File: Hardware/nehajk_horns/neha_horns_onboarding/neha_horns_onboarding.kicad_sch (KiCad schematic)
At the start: 17 parts, among them J1 Conn_01x02_Pin, J2 Conn_01x02_Pin, J3 Conn_01x02_Pin, J4 Conn_01x02_Pin, Q1 IRLZ44N

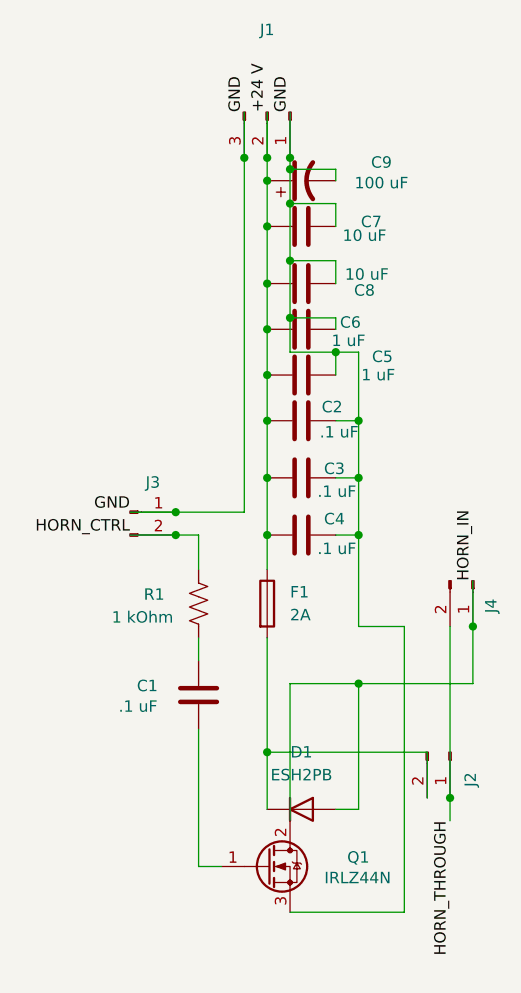
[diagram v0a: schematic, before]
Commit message: Horns PCB with correct connector
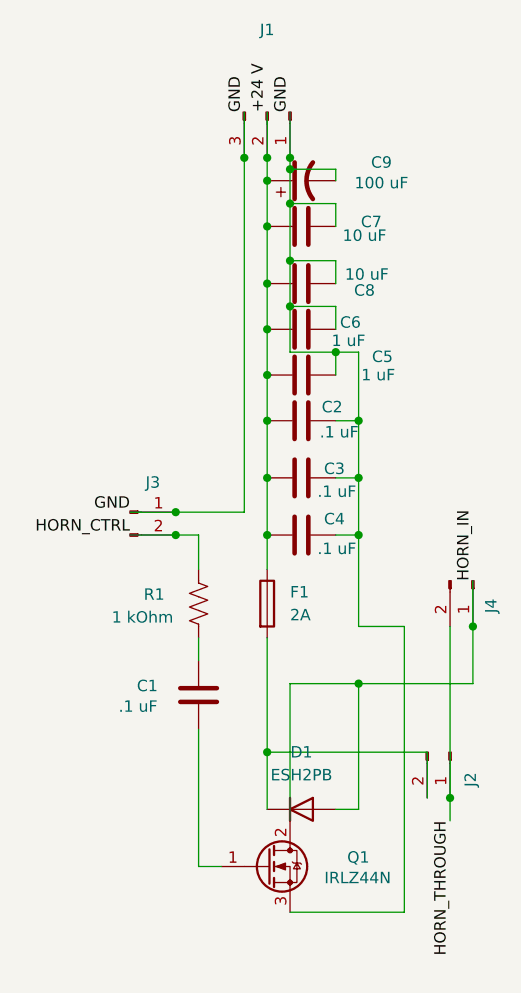
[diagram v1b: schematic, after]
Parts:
- J1: footprint Connector_Molex:Molex_KK-254_AE-6410-03A_1x03_P2.54mm_Vertical -> Connector_Molex:Molex_Micro-Fit_3.0_43650-0300_1x03_P3.00mm_Horizontal
- J2, J3, J4: footprint Connector_Molex:Molex_KK-254_AE-6410-02A_1x02_P2.54mm_Vertical -> Connector_Molex:Molex_Micro-Fit_3.0_43650-0200_1x02_P3.00mm_Horizontal
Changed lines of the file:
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@@
 	)
 	(junction
-		(at 143.51 81.28)
+		(at 143.51 80.01)
 		(diameter 0)
 		(color 0 0 0 0)
@@
 	(wire
 		(pts
-			(xy 143.51 81.28) (xy 143.51 85.09)
+			(xy 143.51 80.01) (xy 143.51 85.09)
 		)
 		(stroke
@@
 	(wire
 		(pts
-			(xy 148.59 81.28) (xy 143.51 81.28)
-		)
-		(stroke
-			(width 0)
-			(type default)
-		)
-	)
-	(wire
-		(pts
-			(xy 143.51 74.93) (xy 143.51 81.28)
+			(xy 148.59 80.01) (xy 143.51 80.01)
+		)
+		(stroke
+			(width 0)
+			(type default)
+		)
+	)
+	(wire
+		(pts
+			(xy 143.51 74.93) (xy 143.51 80.01)
 		)
 		(stroke
@@
 	(wire
 		(pts
-			(xy 148.59 81.28) (xy 148.59 82.55)
+			(xy 148.59 80.01) (xy 148.59 82.55)
 		)
 		(stroke
@@
 			)
 		)
-		(property "Footprint" "Connector_Molex:Molex_KK-254_AE-6410-02A_1x02_P2.54mm_Vertical"
+		(property "Footprint" "Connector_Molex:Molex_Micro-Fit_3.0_43650-0200_1x02_P3.00mm_Horizontal"
 			(at 125.73 102.87 0)
 			(effects
@@
 			)
 		)
-		(property "Footprint" "Connector_Molex:Molex_KK-254_AE-6410-02A_1x02_P2.54mm_Vertical"
+		(property "Footprint" "Connector_Molex:Molex_Micro-Fit_3.0_43650-0200_1x02_P3.00mm_Horizontal"
 			(at 161.29 129.54 0)
 			(effects
@@
 			)
 		)
-		(property "Footprint" "Connector_Molex:Molex_KK-254_AE-6410-02A_1x02_P2.54mm_Vertical"
+		(property "Footprint" "Connector_Molex:Molex_Micro-Fit_3.0_43650-0200_1x02_P3.00mm_Horizontal"
 			(at 163.83 110.49 0)
 			(effects
@@
 			)
 		)
-		(property "Footprint" "Connector_Molex:Molex_KK-254_AE-6410-03A_1x03_P2.54mm_Vertical"
+		(property "Footprint" "Connector_Molex:Molex_Micro-Fit_3.0_43650-0300_1x03_P3.00mm_Horizontal"
 			(at 140.97 58.42 0)
 			(effects

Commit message: corrections made to Horns/LED
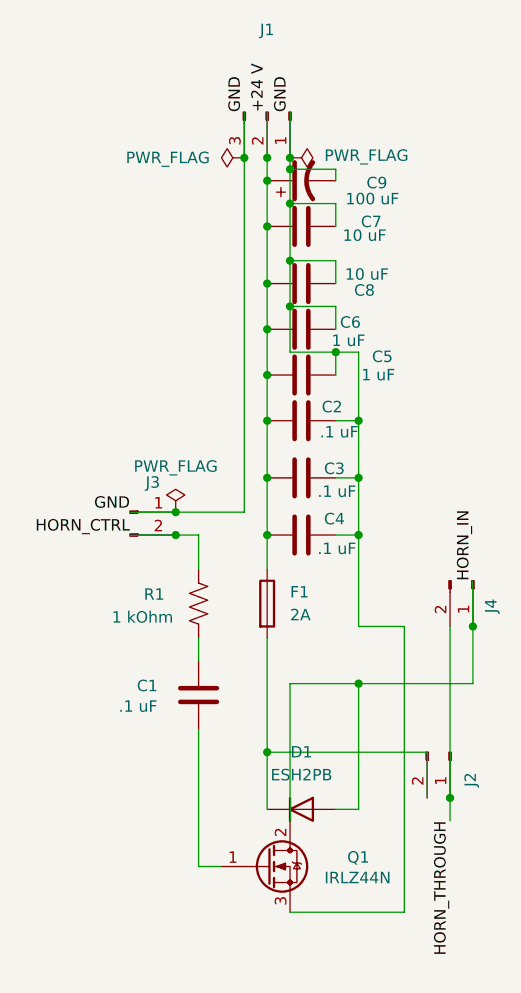
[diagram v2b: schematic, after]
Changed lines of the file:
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@@
+	)
+	(symbol
+		(lib_id "power:PWR_FLAG")
+		(at 138.43 63.5 90)
+		(unit 1)
+		(exclude_from_sim no)
+		(in_bom yes)
+		(on_board yes)
+		(dnp no)
+		(fields_autoplaced yes)
+		(property "Reference" "#FLG2"
+			(at 136.525 63.5 0)
+			(effects
+				(font
+					(size 1.27 1.27)
+				)
+				(hide yes)
+			)
+		)
+		(property "Value" "PWR_FLAG"
+			(at 134.62 63.4999 90)
+			(effects
+				(font
+					(size 1.27 1.27)
+				)
+				(justify left)
+			)
+		)
+		(property "Footprint" ""
+			(at 138.43 63.5 0)
+			(effects
+				(font
+					(size 1.27 1.27)
+				)
+				(hide yes)
+			)
+		)
+		(property "Datasheet" "~"
+			(at 138.43 63.5 0)
+			(effects
+				(font
+					(size 1.27 1.27)
+				)
+				(hide yes)
+			)
+		)
+		(property "Description" "Special symbol for telling ERC where power comes from"
+			(at 138.43 63.5 0)
+			(effects
+				(font
+					(size 1.27 1.27)
+				)
+				(hide yes)
+			)
+		)
+		(pin "1"
+		)
+		(instances
+			(project "neha_horns_onboarding"
+				(path "/55298347-f936-4dfe-8397-61c97f927bbe"
+					(reference "#FLG2")
+					(unit 1)
+				)
+			)
+		)
 	)
 	(symbol
@@
 				(path "/55298347-f936-4dfe-8397-61c97f927bbe"
 					(reference "C2")
+					(unit 1)
+				)
+			)
+		)
+	)
+	(symbol
+		(lib_id "power:PWR_FLAG")
+		(at 143.51 63.5 270)
+		(unit 1)
+		(exclude_from_sim no)
+		(in_bom yes)
+		(on_board yes)
+		(dnp no)
+		(property "Reference" "#FLG3"
+			(at 145.415 63.5 0)
+			(effects
+				(font
+					(size 1.27 1.27)
+				)
+				(hide yes)
+			)
+		)
+		(property "Value" "PWR_FLAG"
+			(at 147.32 63.246 90)
+			(effects
+				(font
+					(size 1.27 1.27)
+				)
+				(justify left)
+			)
+		)
+		(property "Footprint" ""
+			(at 143.51 63.5 0)
+			(effects
+				(font
+					(size 1.27 1.27)
+				)
+				(hide yes)
+			)
+		)
+		(property "Datasheet" "~"
+			(at 143.51 63.5 0)
+			(effects
+				(font
+					(size 1.27 1.27)
+				)
+				(hide yes)
+			)
+		)
+		(property "Description" "Special symbol for telling ERC where power comes from"
+			(at 143.51 63.5 0)
+			(effects
+				(font
+					(size 1.27 1.27)
+				)
+				(hide yes)
+			)
+		)
+		(pin "1"
+		)
+		(instances
+			(project "neha_horns_onboarding"
+				(path "/55298347-f936-4dfe-8397-61c97f927bbe"
+					(reference "#FLG3")
+					(unit 1)
+				)
+			)
+		)
+	)
+	(symbol
+		(lib_id "power:PWR_FLAG")
+		(at 130.81 102.87 0)
+		(unit 1)
+		(exclude_from_sim no)
+		(in_bom yes)
+		(on_board yes)
+		(dnp no)
+		(fields_autoplaced yes)
+		(property "Reference" "#FLG1"
+			(at 130.81 100.965 0)
+			(effects
+				(font
+					(size 1.27 1.27)
+				)
+				(hide yes)
+			)
+		)
+		(property "Value" "PWR_FLAG"
+			(at 130.81 97.79 0)
+			(effects
+				(font
+					(size 1.27 1.27)
+				)
+			)
+		)
+		(property "Footprint" ""
+			(at 130.81 102.87 0)
+			(effects
+				(font
+					(size 1.27 1.27)
+				)
+				(hide yes)
+			)
+		)
+		(property "Datasheet" "~"
+			(at 130.81 102.87 0)
+			(effects
+				(font
+					(size 1.27 1.27)
+				)
+				(hide yes)
+			)
+		)
+		(property "Description" "Special symbol for telling ERC where power comes from"
+			(at 130.81 102.87 0)
+			(effects
+				(font
+					(size 1.27 1.27)
+				)
+				(hide yes)
+			)
+		)
+		(pin "1"
+		)
+		(instances
+			(project ""
+				(path "/55298347-f936-4dfe-8397-61c97f927bbe"
+					(reference "#FLG1")
 					(unit 1)
 				)
@@
 		(dnp no)
 		(property "Reference" "C9"
-			(at 153.67 64.008 90)
+			(at 153.162 66.294 90)
 			(effects
 				(font
@@
 		)
 		(property "Value" "100 uF"
-			(at 153.67 66.294 90)
-			(effects
-				(font
+			(at 152.654 68.072 90)
+			(effects
+				(font
